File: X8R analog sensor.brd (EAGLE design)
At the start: 25.1 x 8.9 mm, 13 parts, among them IC1 MCP1703CB, U1 ATTINY13SOIC

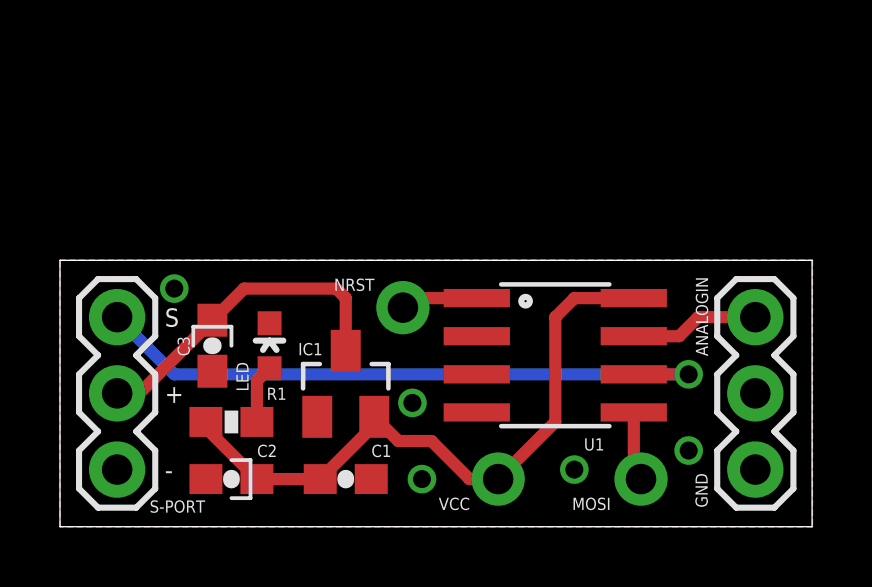
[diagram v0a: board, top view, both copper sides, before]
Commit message: updated for voltage divider, and ISP interface
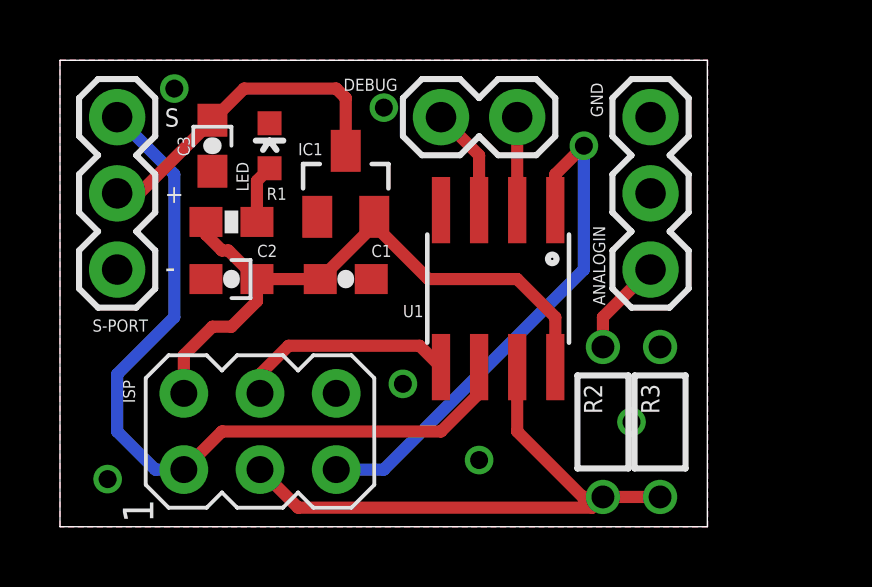
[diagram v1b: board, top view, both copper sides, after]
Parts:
- removed MOSI, NRST, VCC: (no value), adafruit:1X01-CLEANBIG
- added DEBUG: M02PTH, SparkFun-Connectors:1X02
- added ISP: AVRISP-6, adafruit:AVRISP
- added R2, R3: (no value), SparkFun-Passives:1/6W-RES
- LED: value (none) -> BLUE
- moved C1 6.67 mm to (9.53, 8.26)
- moved C2 6.67 mm to (5.71, 8.26)
- moved R1 6.67 mm to (5.71, 10.2)
- moved C3 6.67 mm to (5.08, 12.7)
- moved IC1 6.67 mm to (9.53, 11.4)
- moved LED 6.67 mm to (6.99, 12.7)
- moved S-PORT 6.67 mm to (1.91, 8.57)
- moved ANALOGIN 3.84 mm to (19.7, 8.57), turned to 90 degrees
- moved U1 2.93 mm to (14.6, 7.94), turned to 180 degrees
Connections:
- net N$2 renamed VIN
- removed net N$3: S-PORT.3, U1.6
- removed net N$4: ANALOGIN.1, U1.7
- removed net N$5: MOSI.1, U1.5
- removed net N$6: C1.1, C2.1, IC1.2, R1.2, U1.8, VCC.1
- removed net N$8: NRST.1, U1.1
- new net ADC2: DEBUG.1, U1.3
- new net ADC3: DEBUG.2, U1.2
- new net AIN: ANALOGIN.1, R2.2
- new net AIN-O: ISP.3, R2.1, R3.2, U1.7
- new net MOSI: ISP.4, U1.5
- new net NRES: ISP.5, U1.1
- new net SPORT: ISP.1, S-PORT.3, U1.6
- new net VCC: C1.1, C2.1, IC1.2, ISP.2, R1.2, U1.8
- net GND: now also ISP.6, R3.1
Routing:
- net SPORT: track 0.00 -> 26.6 mm
- net VCC: track 0.00 -> 21.8 mm
- net N$3: track 21.7 -> 0.00 mm, vias 1 -> 0
- net N$6: track 21.6 -> 0.00 mm
- net AIN-O: track 0.00 -> 19.9 mm
- net NRES: track 0.00 -> 17.7 mm, vias 0 -> 1
- net MOSI: track 0.00 -> 7.36 mm
- net N$4: track 4.31 -> 0.00 mm
- net ADC2: track 0.00 -> 3.62 mm
- net AIN: track 0.00 -> 3.24 mm
- net ADC3: track 0.00 -> 3.10 mm
- net N$8: track 2.60 -> 0.00 mm
- net N$5: track 2.32 -> 0.00 mm
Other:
- board size 25.1 x 8.9 mm -> 21.6 x 15.5 mm
- board text added: "20131022-1"
- board text added: "X8R S.port-2-analog"
